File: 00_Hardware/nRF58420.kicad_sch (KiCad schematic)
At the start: 34 parts, among them IC2 E22-900M22S, J5 SMA_ST_SMD, U5 nRF52840-QFAA, Y1 Crystal

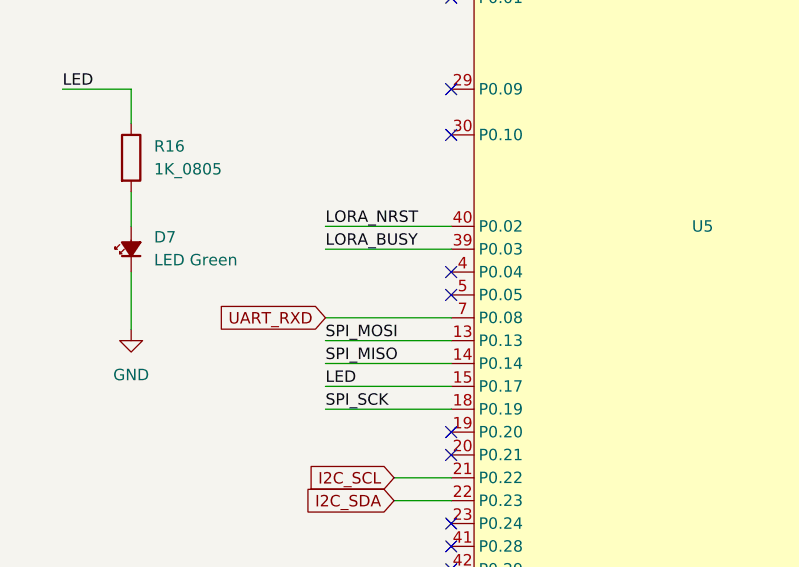
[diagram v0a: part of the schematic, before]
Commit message: Removed SMA for GPIO header placement.
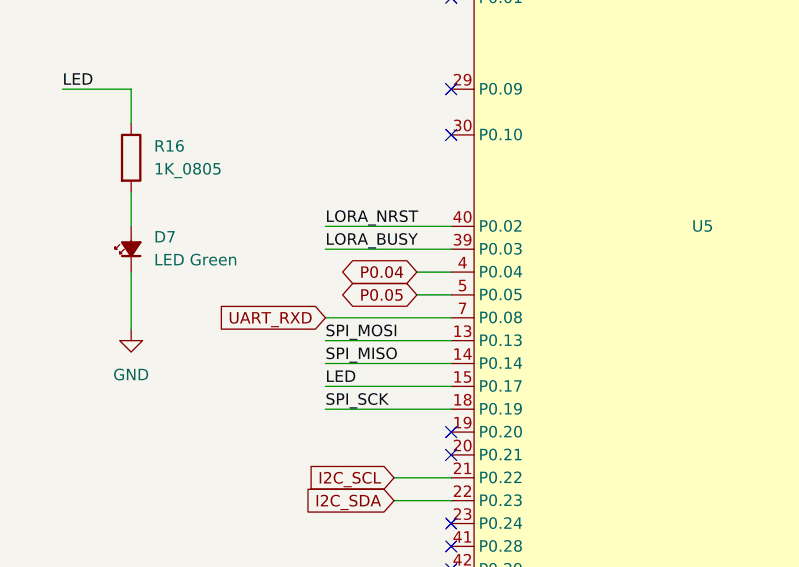
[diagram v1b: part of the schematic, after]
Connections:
- net P0.04: now reaches U5.4 (P0.04)
- net P0.05: now reaches U5.5 (P0.05)
- no-connect marks 18 -> 16
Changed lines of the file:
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@@
+	)
+	(no_connect
+		(at 66.04 92.71)
 	)
 	(no_connect
@@
 	)
 	(no_connect
-		(at 66.04 92.71)
-	)
-	(no_connect
 		(at 125.73 135.89)
 	)
@@
 	)
 	(no_connect
-		(at 66.04 113.03)
-	)
-	(no_connect
-		(at 66.04 115.57)
-	)
-	(no_connect
 		(at 66.04 82.55)
 	)
@@
 	(wire
 		(pts
+			(xy 62.23 115.57) (xy 66.04 115.57)
+		)
+		(stroke
+			(width 0)
+			(type default)
+		)
+	)
+	(wire
+		(pts
 			(xy 135.89 115.57) (xy 135.89 118.11)
 		)
@@
 		(pts
 			(xy 184.15 64.77) (xy 198.12 64.77)
+		)
+		(stroke
+			(width 0)
+			(type default)
+		)
+	)
+	(wire
+		(pts
+			(xy 62.23 113.03) (xy 66.04 113.03)
 		)
 		(stroke
@@
 		)
 	)
+	(global_label "P0.05"
+		(shape bidirectional)
+		(at 62.23 115.57 180)
+		(fields_autoplaced yes)
+		(effects
+			(font
+				(size 1.27 1.27)
+			)
+			(justify right)
+		)
+		(property "Intersheetrefs" "${INTERSHEET_REFS}"
+			(at 52.6302 115.57 0)
+			(effects
+				(font
+					(size 1.27 1.27)
+				)
+				(justify right)
+				(hide yes)
+			)
+		)
+	)
 	(global_label "UART_TXD"
 		(shape input)
@@
 			(effects
 				(font
+					(size 1.27 1.27)
+				)
+				(justify right)
+				(hide yes)
+			)
+		)
+	)
+	(global_label "P0.04"
+		(shape bidirectional)
+		(at 62.23 113.03 180)
+		(fields_autoplaced yes)
+		(effects
+			(font
+				(size 1.27 1.27)
+			)
+			(justify right)
+		)
+		(property "Intersheetrefs" "${INTERSHEET_REFS}"
+			(at 52.6302 113.03 0)
+			(effects
+				(font

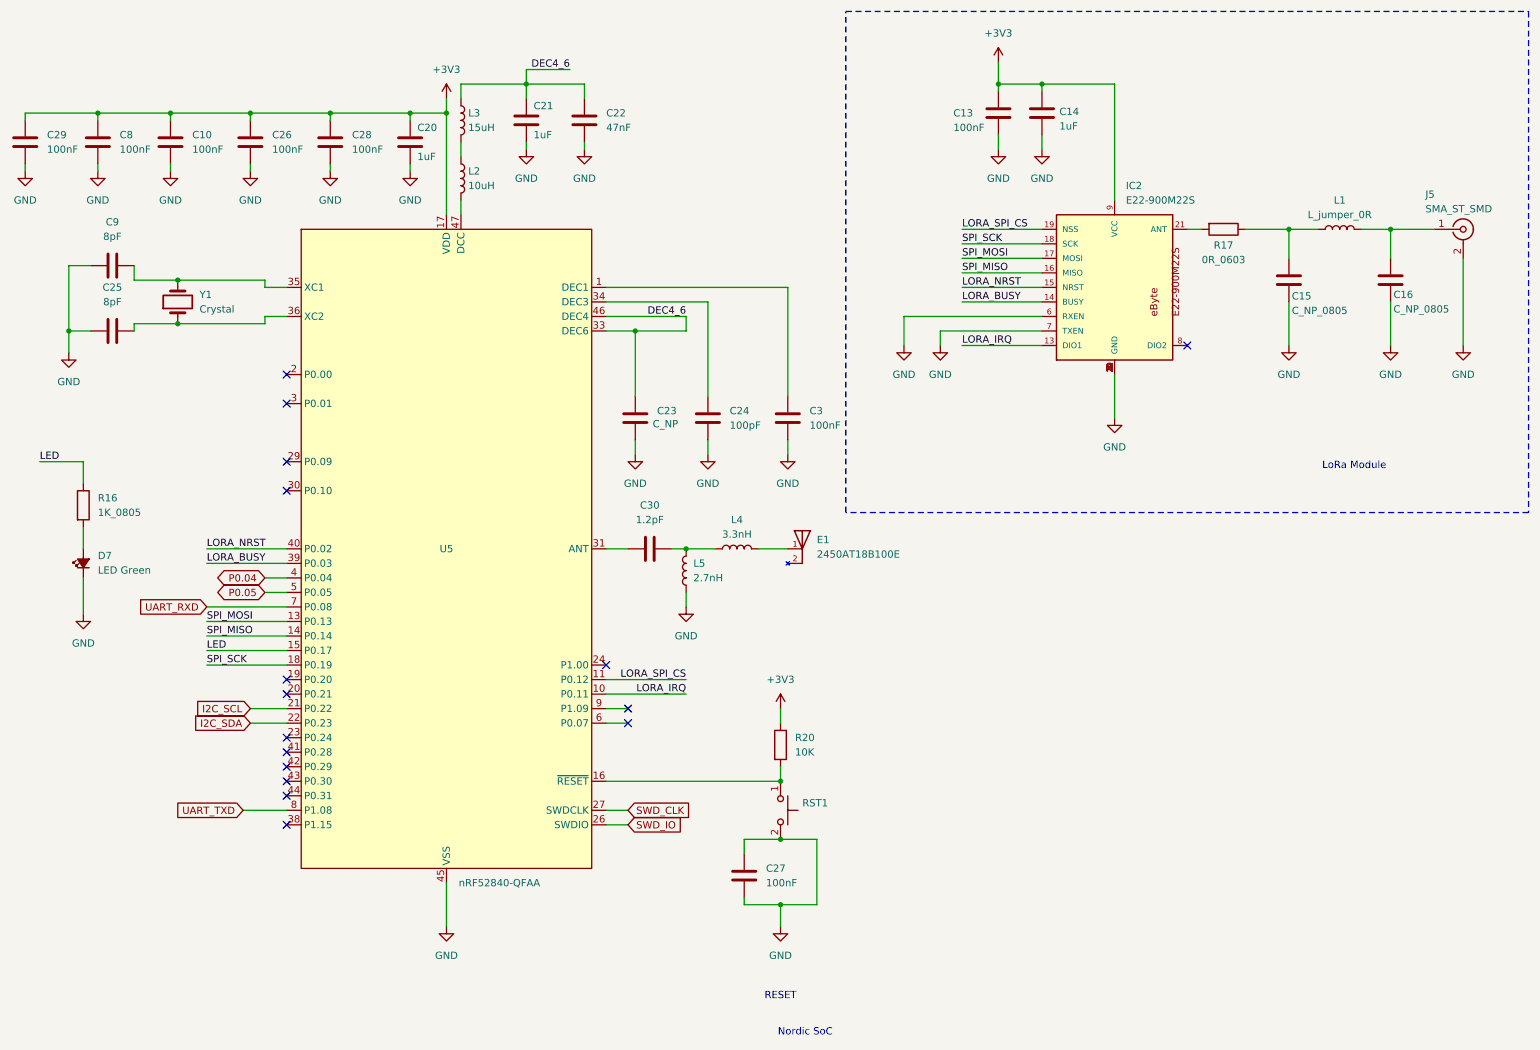
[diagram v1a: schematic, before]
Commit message: Antenna output changed to fully isolate path
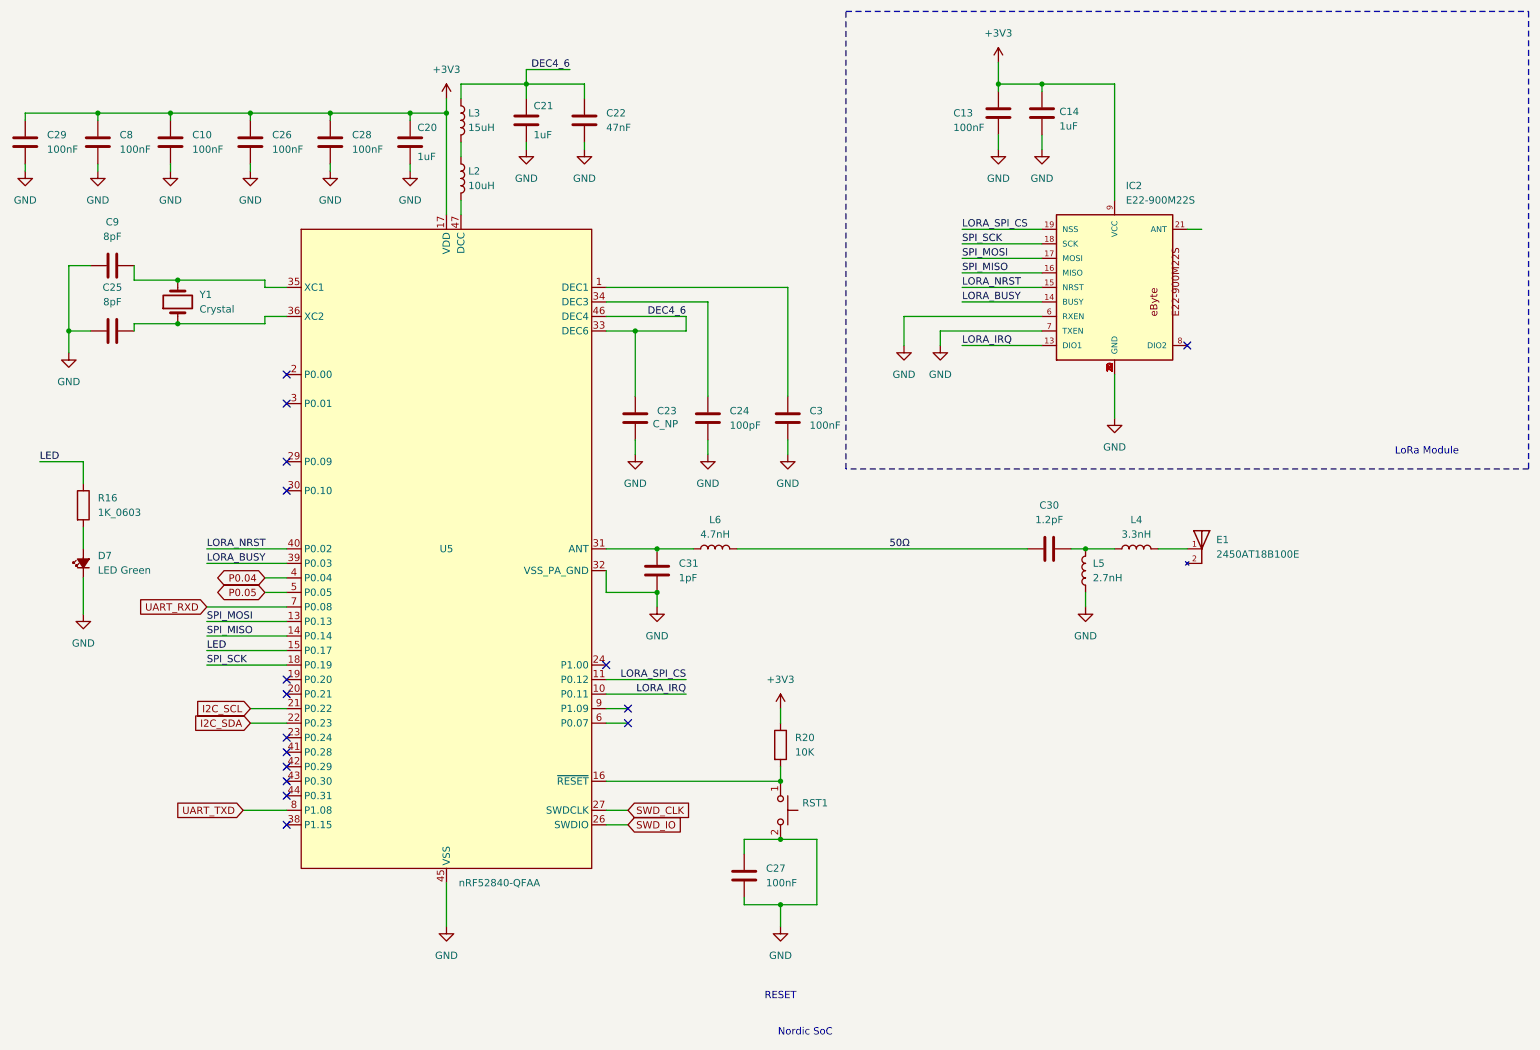
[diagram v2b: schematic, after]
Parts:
- removed C15, C16: C_NP_0805, Project_Footprints:C_0805_2012Metric, symbol Library:C_NP_0805
- removed J5: SMA_ST_SMD, Project_Footprints:SMA_ST_SMD, symbol Library:SMA_ST_SMD
- removed L1: L_jumper_0R, Project_Footprints:L_0805_2012Metric, symbol Library:L_jumper_0R
- removed R17: 0R_0603, Resistor_SMD:R_0603_1608Metric, symbol IBA_resistors:0R_0603
- added C31: 1pF, Capacitor_SMD:C_0402_1005Metric, symbol Device:C
- added L6: 4.7nH, Inductor_SMD:L_0402_1005Metric, symbol Device:L
- R16: value 1K_0805 -> 1K_0603; footprint Project_Footprints:R_0805_2012Metric -> Resistor_SMD:R_0603_1608Metric; MPN1 CRCW08051K00FKEA -> (none); MPN2 ERJ6ENF1001V -> (none); Mfr1 Vishay -> (none); Mfr2 Panasonic -> (none); Status Preferred -> (none)
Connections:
- net GND: now also C31.2
- net at U5.31 (ANT): now also C31.1, L6.1; no longer C30.1
- new net 50Ω: C30.1, L6.2
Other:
- moved on the sheet: C30, E1, L4, L5

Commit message: updated from generated script
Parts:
- C3: LCSC (none) -> C14663
- E1: Mfr1 (none) -> Johanson Technology
- IC2: Description_1 SX1262 868/915MHz SPI SMD LoRa Module -> (none); MF EBYTE -> (none)
- L5: MFR1 Johanson Technology -> (none)
- R16: value 1K_0603 -> 1k
- R20: value 10K -> 10k
